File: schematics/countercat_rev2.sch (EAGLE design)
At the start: 32 parts, among them Q1 2N3904, Q2 IRF520, U2 74HC04_HEX_INVERTER, U3 USD-SOCKETNEW, U4 ATMEGA328P_PDIP, Y1 16MHz

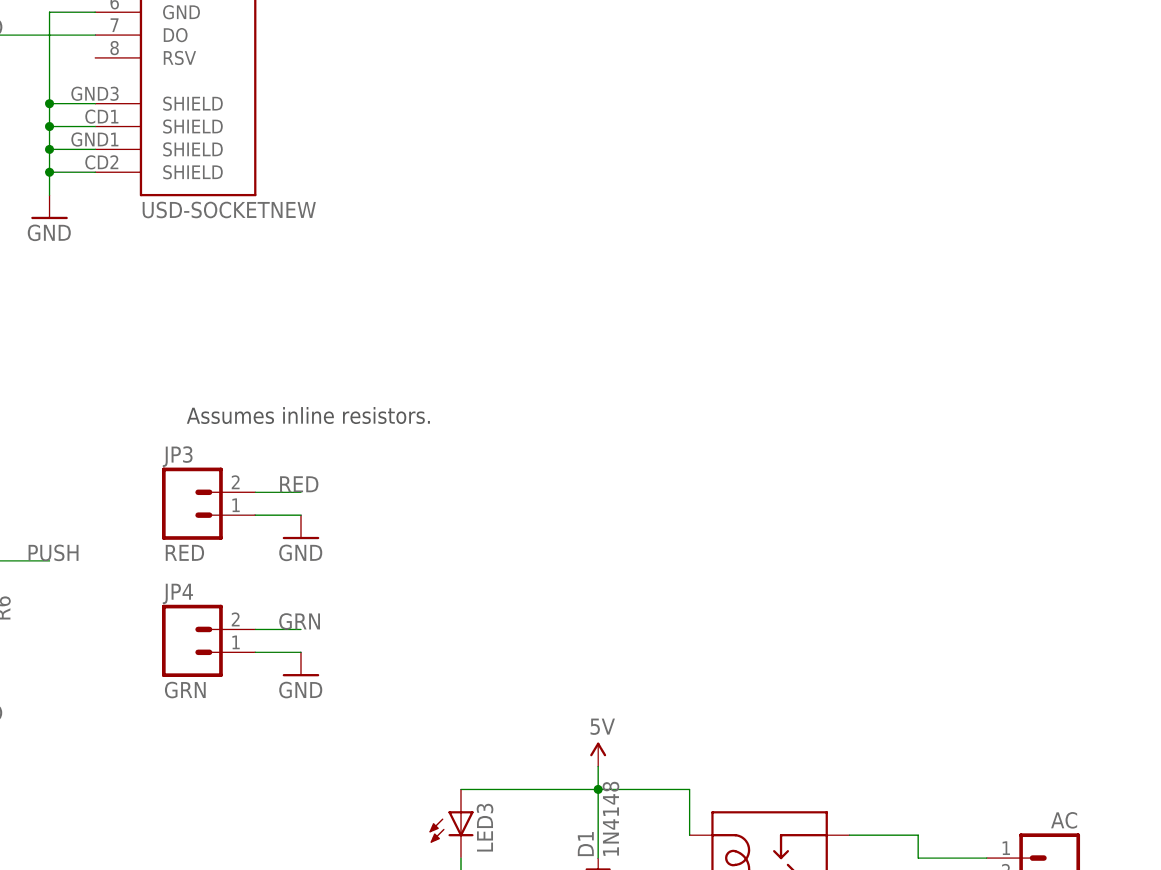
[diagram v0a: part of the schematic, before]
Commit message: Changed the LED hookup schematic
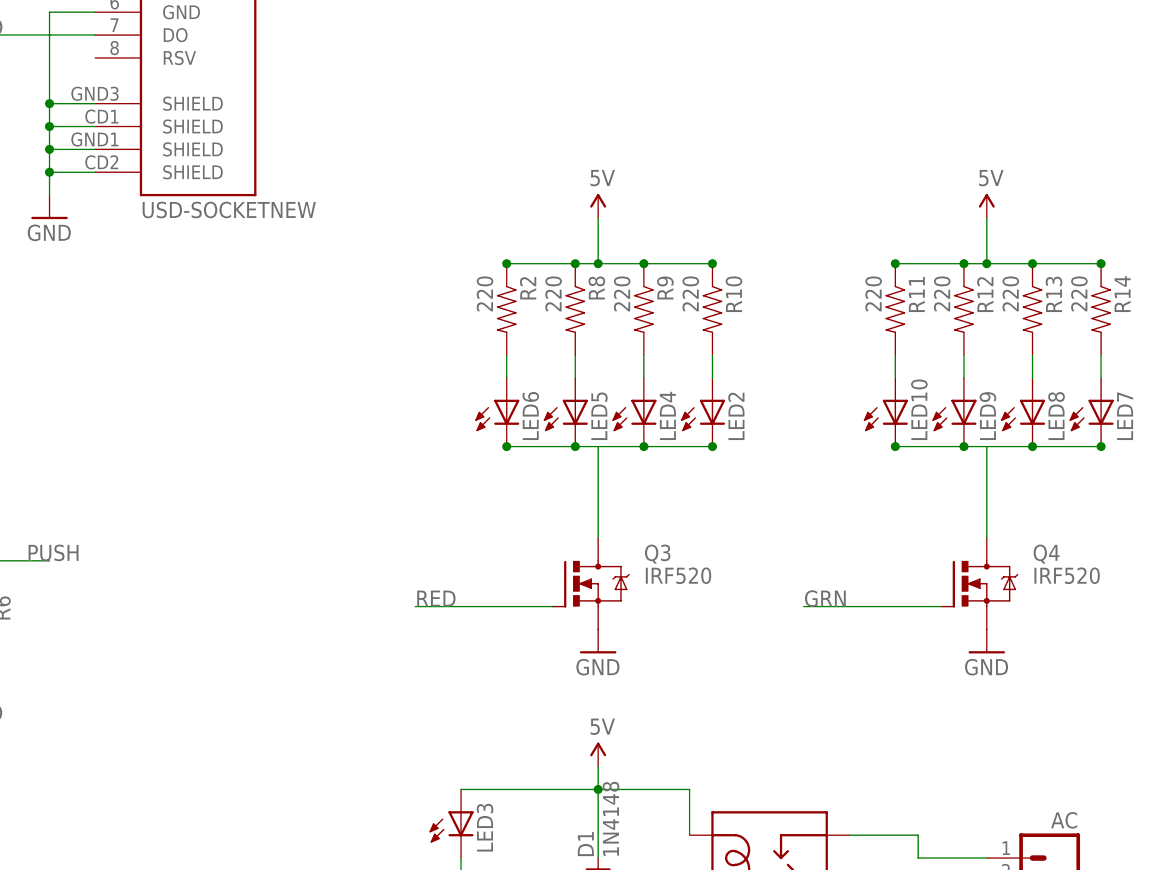
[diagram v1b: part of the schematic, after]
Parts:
- removed JP3: RED, SparkFun:M02POLAR
- removed JP4: GRN, SparkFun:M02POLAR
- added LED10, LED2, LED4, LED5, LED6, LED7, LED8, LED9: (no value), nick_DC2011:LED3MM
- added Q3, Q4: IRF520, transistor-power:IRF520
- added R10, R11, R12, R13, R14, R2, R8, R9: 220, SparkFun-Resistors:RESISTORPTH-1/4W
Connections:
- new net N$18: LED6.A, R2.2
- new net N$19: LED5.A, R8.2
- new net N$2: LED2.C, LED4.C, LED5.C, LED6.C, Q3.D
- new net N$21: LED4.A, R9.2
- new net N$22: LED2.A, R10.2
- new net N$23: LED10.C, LED7.C, LED8.C, LED9.C, Q4.D
- new net N$24: LED10.A, R11.2
- new net N$25: LED9.A, R12.2
- new net N$26: LED8.A, R13.2
- new net N$27: LED7.A, R14.2
- net 5V: now also R10.1, R11.1, R12.1, R13.1, R14.1, R2.1, R8.1, R9.1
- net GND: now also Q3.S, Q4.S; no longer JP3.1, JP4.1
- net GRN: now also Q4.G; no longer JP4.2
- net RED: now also Q3.G; no longer JP3.2
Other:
- note removed: "Assumes inline resistors."

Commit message: Started board design
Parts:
- removed C1, C4: .1uF, SparkFun-Capacitors:CAPPTH2
- removed D1: 1N4148, SparkFun:DIODEPTH
- removed LED1: Red, SparkFun-LED:LED3MM
- removed LED10, LED2, LED3, LED4, LED5, LED6, LED7, LED8, LED9: (no value), nick_DC2011:LED3MM
- removed LM7805: 5v, SparkFun-PowerIC:V_REG_78XXSINK
- removed MCP1700-3302E: 3.3v, SparkFun-PowerIC:V_REG_78XXTO-92_UNTESTED
- removed Q1: 2N3904, SparkFun:TRANSISTOR_NPNTO92
- removed Q2: IRF520, transistor-power:IRF520
- removed R1, R3, R5: 1k, SparkFun-Resistors:RESISTORPTH-1/4W
- removed R4: 10k, SparkFun-Resistors:RESISTORPTH-1/4W
- removed U$2: RELAYPTH3, SparkFun:RELAYPTH3
- removed U2: 74HC04_HEX_INVERTER, SparkFun-DigitalIC:74HC04_HEX_INVERTER
- removed U3: USD-SOCKETNEW, SparkFun:USD-SOCKETNEW
- added JP11: GRN1, SparkFun:M02POLAR
- added JP12: GRN2, SparkFun:M02POLAR
- added JP13: GRN3, SparkFun:M02POLAR
- added JP14: GRN4, SparkFun:M02POLAR
- added JP3: RED1, SparkFun:M02POLAR
- added JP4: RED2, SparkFun:M02POLAR
- JP2: value AC -> RELAY; device NickDC2011Breakouts:M025MM -> SparkFun:M03POLAR
- JP7: value VC0706 -> RED3; device SparkFun-Connectors:M04POLAR -> SparkFun:M02POLAR
- JP8: value FLASH -> RED4
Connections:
- removed net 3.3V: C4.1, LED1.A, MCP1700-3302E.OUT, U2.VCC, U3.VCC
- removed net N$1: LED3.C, R3.1
- removed net N$10: D1.A, Q1.C, R3.2, U$2.COIL2
- removed net N$11: Q1.B, R4.1, R5.2
- removed net N$14: LED1.C, R1.2
- removed net N$17: U2.5Y, U2.6A
- removed net N$20: U2.2Y, U3.CS
- removed net N$23: LED10.C, LED7.C, LED8.C, LED9.C, Q4.D
- removed net N$24: LED10.A, R11.2
- removed net N$25: LED9.A, R12.2
- removed net N$26: LED8.A, R13.2
- removed net N$27: LED7.A, R14.2
- removed net N$6: JP2.1, U$2.NC
- removed net N$9: JP2.2, U$2.NO
- removed net VB: JP10.2, LM7805.IN
- net 5V: now also JP10.2, JP2.1; no longer C1.1, D1.C, JP7.4, JP8.1, LED3.A, LM7805.OUT, MCP1700-3302E.IN, U$2.COIL1
- net FLASH: no longer Q2.G
- net GND: now also JP2.2; no longer C1.2, C4.2, JP7.3, LM7805.GND, MCP1700-3302E.GND, Q1.E, Q2.S, R1.1, R4.2, U2.GND, U3.GND, U3.SHIELD@1, U3.SHIELD@2, U3.SHIELD@3, U3.SHIELD@4
- net N$13: now also JP12.2, R12.2; no longer U2.4Y, U3.DI
- net N$15: now also JP13.2, R13.2; no longer U2.6Y, U3.SCK
- net N$16: now also JP14.2, R14.2; no longer U2.3Y, U2.4A
- net N$18: now also JP3.2; no longer LED6.A
- net N$19: now also JP4.2; no longer LED5.A
- net N$2: now also JP3.1, JP4.1, JP7.1, JP8.1; no longer LED2.C, LED4.C, LED5.C, LED6.C
- net N$21: now also JP7.2; no longer LED4.A
- net N$22: now also JP8.2; no longer LED2.A
- net N$4: now also JP11.1, JP12.1, JP13.1, JP14.1; no longer JP8.2, Q2.D
- net N$5: now also JP11.2, R11.2; no longer U2.1Y, U2.2A
- net RELAY: now also JP2.3; no longer R5.1
- net SFW_RXI: no longer JP7.1
- net SFW_TXO: no longer JP7.2
- net SPI_CS: no longer U2.1A
- net SPI_MISO: no longer U3.DO
- net SPI_MOSI: no longer U2.3A
- net SPI_SCK: no longer U2.5A
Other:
- note removed: "Attach 12 IR LEDs in parallel"
- note removed: "CAMERA"
- note removed: "Power Indicator"
- moved on the sheet: JP8, Q4, R10, R11, R12, R13, R14, R2, R8, R9

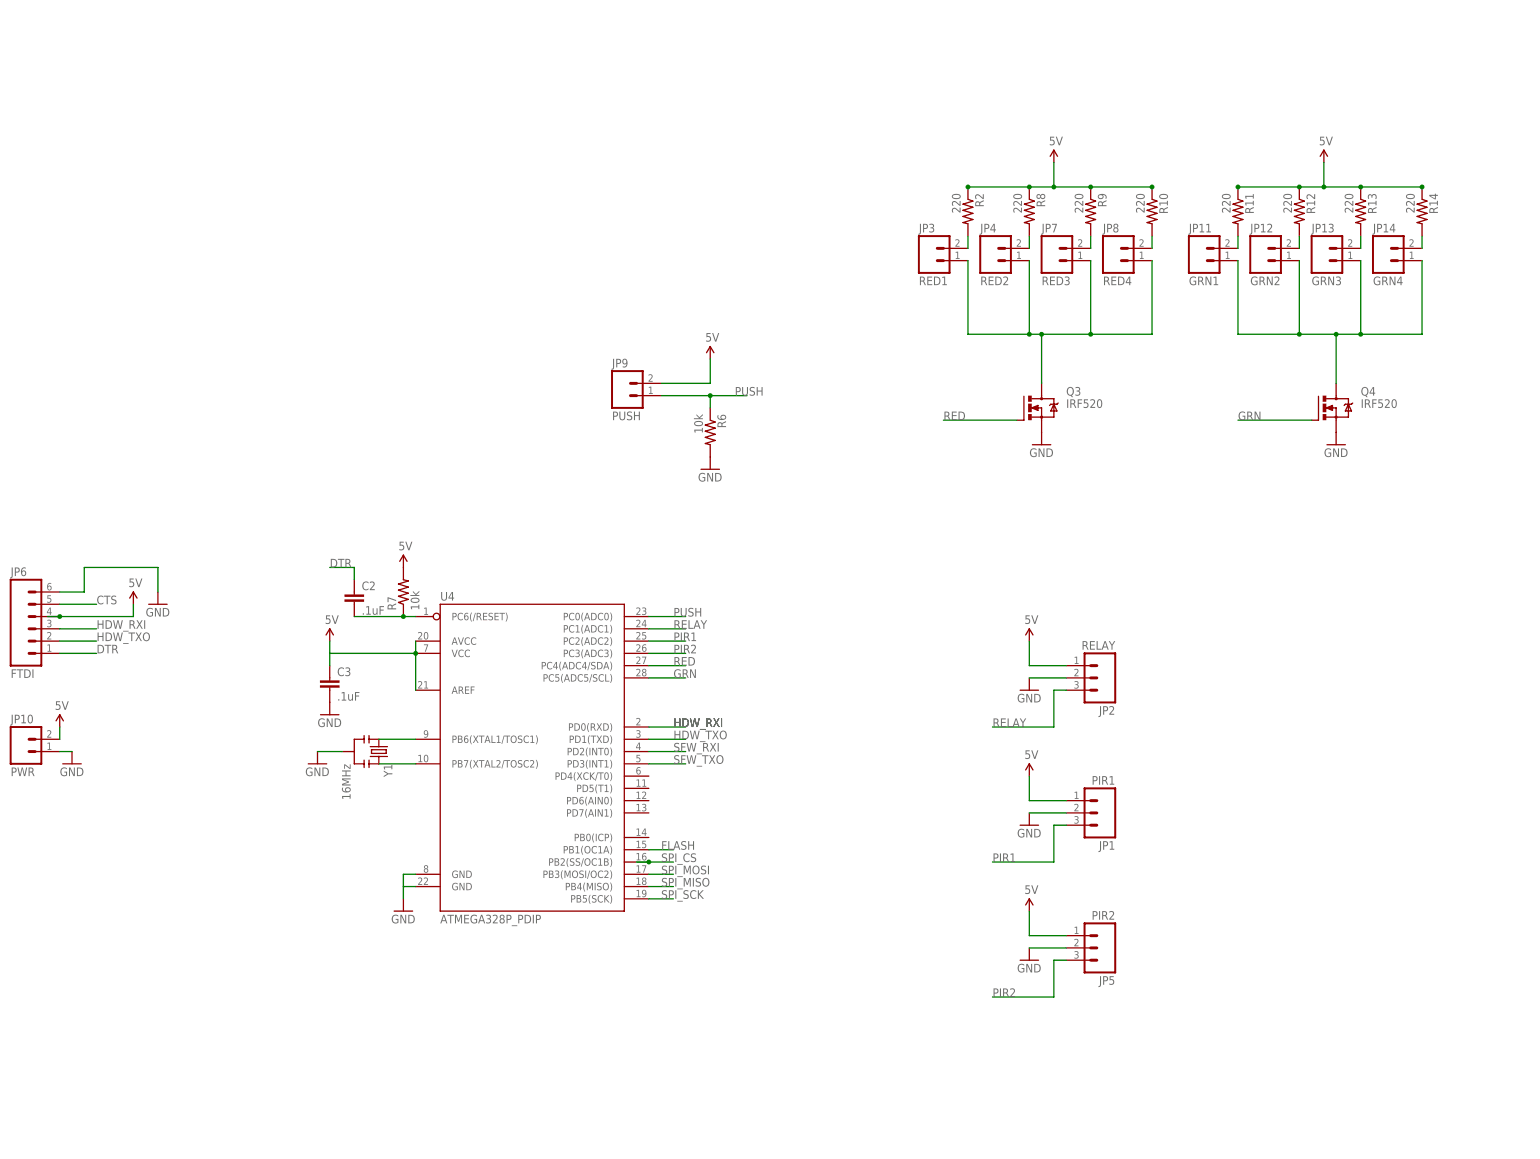
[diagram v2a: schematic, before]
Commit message: Changed board size, add shifter
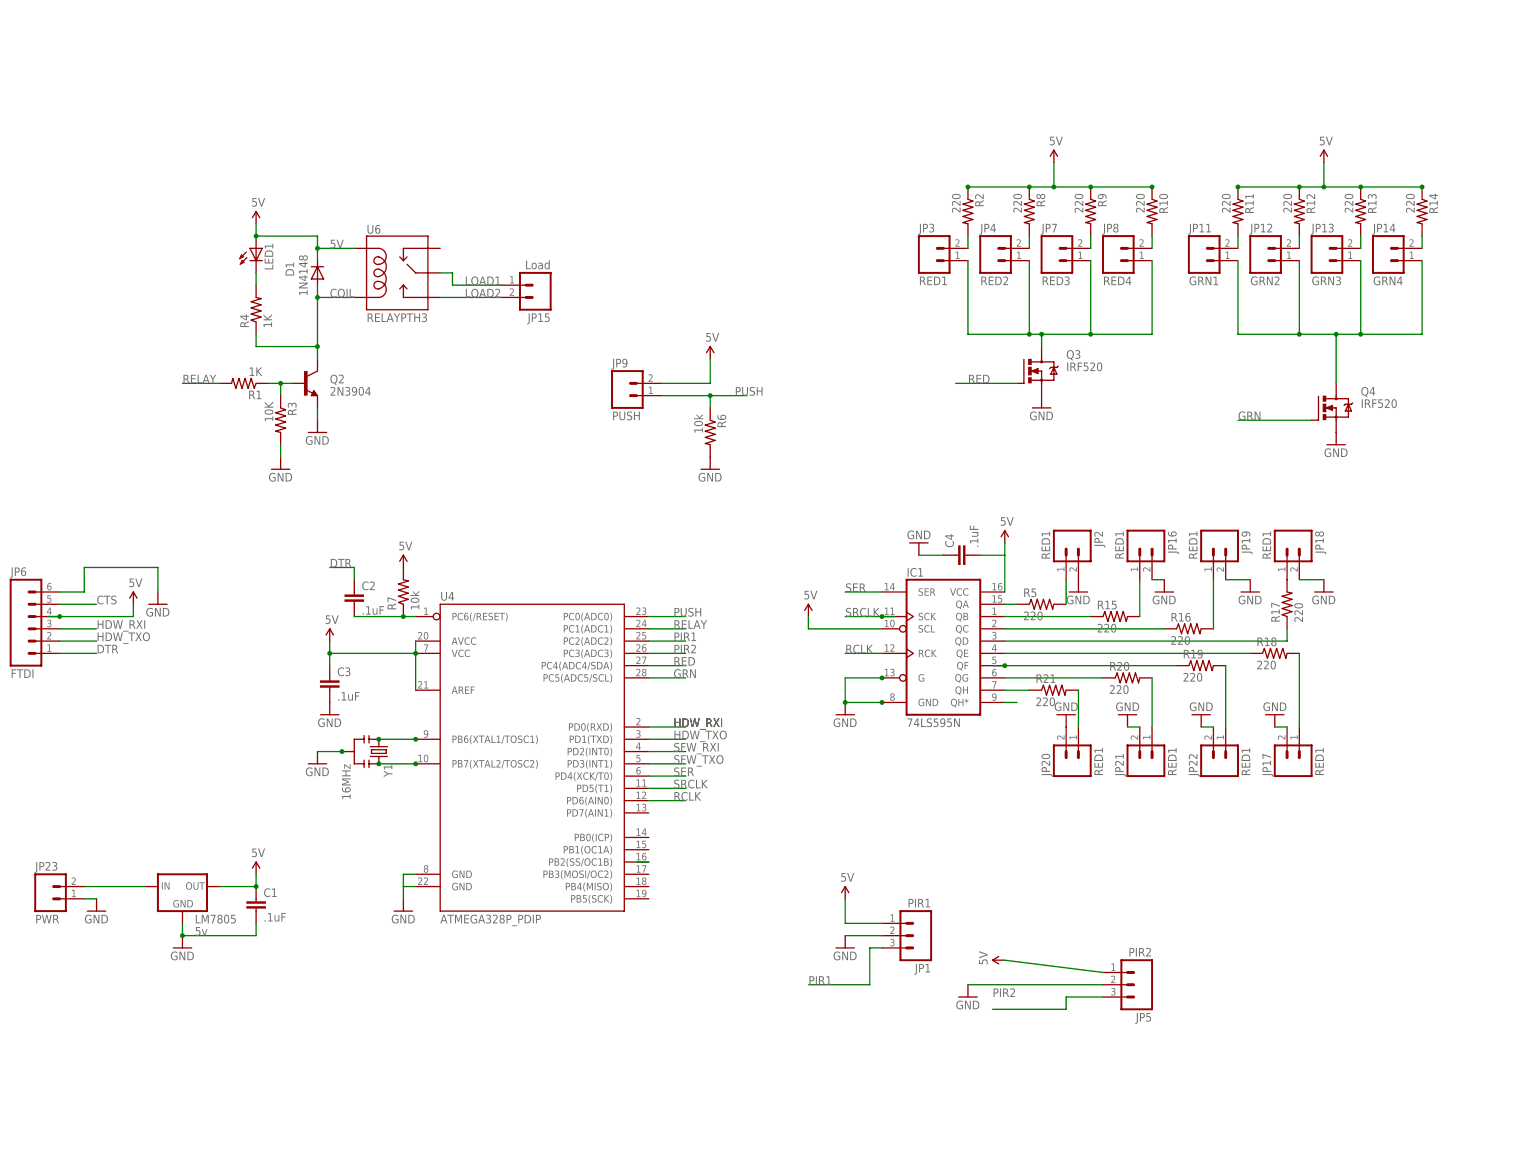
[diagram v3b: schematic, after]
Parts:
- removed JP10: PWR, SparkFun:M02POLAR
- added C1, C4: .1uF, SparkFun-Capacitors:CAPPTH2
- added D1: 1N4148, SparkFun:DIODE1N4148
- added IC1: 74LS595N, SparkFun-DigitalIC:74LS595N
- added JP15: Load, SparkFun:M025MM
- added JP16, JP17, JP18, JP19, JP20, JP21, JP22: RED1, SparkFun:M02POLAR
- added JP23: PWR, SparkFun:M02POLAR
- added LED1: (no value), SparkFun:LED5MM
- added LM7805: 5v, SparkFun-PowerIC:V_REG_78XXSINK
- added Q2: 2N3904, SparkFun:TRANSISTOR_NPNTO92
- added R1, R4: 1K, SparkFun-Resistors:RESISTORPTH-1/4W
- added R15, R16, R17, R18, R19, R20, R21, R5: 220, SparkFun-Resistors:RESISTORPTH-1/4W
- added R3: 10K, SparkFun-Resistors:RESISTORPTH-1/4W
- added U6: RELAYPTH3, SparkFun:RELAYPTH3
- JP2: value RELAY -> RED1; device SparkFun:M03POLAR -> SparkFun:M02POLAR
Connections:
- removed net FLASH: U4.PB1(OC1A)
- removed net N$12: C3.1
- removed net SPI_MISO: U4.PB4(MISO)
- removed net SPI_MOSI: U4.PB3(MOSI/OC2)
- removed net SPI_SCK: U4.PB5(SCK)
- new net COIL: D1.A, Q2.C, R4.1, U6.COIL2
- new net LOAD1: JP15.1, U6.MAIN
- new net LOAD2: JP15.2, U6.NO
- new net N$1: IC1.QH*
- new net N$10: JP2.1, R5.2
- new net N$11: JP16.1, R15.2
- new net N$14: JP19.1, R16.2
- new net N$17: JP18.1, R17.2
- new net N$20: JP17.1, R18.2
- new net N$23: JP22.1, R19.2
- new net N$24: JP21.1, R20.2
- new net N$25: JP20.1, R21.2
- new net N$26: IC1.QA, R5.1
- new net N$27: IC1.QB, R15.1
- new net N$28: IC1.QC, R16.1
- new net N$29: IC1.QD, R17.1
- new net N$30: IC1.QE, R18.1
- new net N$31: IC1.QF, R19.1
- new net N$32: IC1.QG, R20.1
- new net N$33: IC1.QH, R21.1
- new net N$6: Q2.B, R1.1, R3.1
- new net N$9: LED1.C, R4.2
- new net RCLK: IC1.RCK, U4.PD6(AIN0)
- new net SER: IC1.SER, U4.PD4(XCK/T0)
- new net SRCLK: IC1.SCK, U4.PD5(T1)
- new net VB: JP23.2, LM7805.IN
- net 5V: now also C1.1, C4.2, D1.C, IC1.SCL, IC1.VCC, LED1.A, LM7805.OUT, U6.COIL1; no longer JP10.2, JP2.1
- net GND: now also C1.2, C4.1, IC1.G, IC1.GND, JP16.2, JP17.2, JP18.2, JP19.2, JP20.2, JP21.2, JP22.2, JP23.1, LM7805.GND, Q2.E, R3.2; no longer JP10.1
- net N$8: now also C3.1
- net RELAY: now also R1.2; no longer JP2.3
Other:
- moved on the sheet: JP1, JP5, Q3

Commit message: Updated board and schematic
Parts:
- removed R10, R12, R13, R14, R15, R16, R17, R18, R19, R20, R21, R5: 220, SparkFun-Resistors:RESISTORPTH-1/4W
- added BLU, GRN, RED, YLW: (no value), SparkFun-LED:LED3MM
- added C5: .1uF, SparkFun-Capacitors:CAPPTH2
- added JP10: RED_RAW, SparkFun:M02POLAR
- added JP24: GRN_RAW, SparkFun:M02POLAR
- added JP25: BLU1, SparkFun:M02POLAR
- added JP26: BLU2, SparkFun:M02POLAR
- added JP27: BLU3, SparkFun:M02POLAR
- added JP28: BLU4, SparkFun:M02POLAR
- added JP29: BLU_RAW, SparkFun:M02POLAR
- added JP30: YLW1, SparkFun:M02POLAR
- added JP31: YLW2, SparkFun:M02POLAR
- added JP32: YLW3, SparkFun:M02POLAR
- added JP33: YLW4, SparkFun:M02POLAR
- added JP34: YLW_RAW, SparkFun:M02POLAR
- added JP35: AUX, SparkFun-Connectors:M08LOCK
- added JP36: AUX_PWR, SparkFun:M02POLAR
- added Q1, Q5: IRF520, transistor-power:IRF520
- added R35: R-GRN, SparkFun-Resistors:RPACK-BUSSED-5-SIP-PTH-5
- JP16: value RED1 -> SHF3
- JP17: value RED1 -> SHF5
- JP18: value RED1 -> SHF1
- JP19: value RED1 -> SHF2
- JP2: value RED1 -> SHF4
- JP20: value RED1 -> SHF8
- JP21: value RED1 -> SHF7
- JP22: value RED1 -> SHF6
- R11: value 220 -> R-SHF; device SparkFun-Resistors:RESISTORPTH-1/4W -> SparkFun-Resistors:RPACK-BUSSED-8-SIP-PTH-8
- R2: value 220 -> R-RED; device SparkFun-Resistors:RESISTORPTH-1/4W -> SparkFun-Resistors:RPACK-BUSSED-5-SIP-PTH-5
- R8: value 220 -> R-BLU; device SparkFun-Resistors:RESISTORPTH-1/4W -> SparkFun-Resistors:RPACK-BUSSED-5-SIP-PTH-5
- R9: value 220 -> R-YLW; device SparkFun-Resistors:RESISTORPTH-1/4W -> SparkFun-Resistors:RPACK-BUSSED-5-SIP-PTH-5
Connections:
- removed net N$22 (its old number): JP8.2, R10.2
- removed net SFW_RXI: U4.PD2(INT0)
- removed net SFW_TXO: U4.PD3(INT1)
- new net B0: JP35.3, U4.PB0(ICP)
- new net B1: JP35.4, U4.PB1(OC1A)
- new net BLU: Q3.G, U4.PD2(INT0)
- new net D7: JP35.2, U4.PD7(AIN1)
- new net N$12: JP4.2, R2.3
- new net N$18: JP7.2, R2.4
- new net N$34: BLU.C, JP25.1, JP26.1, JP27.1, JP28.1, JP29.1, Q3.D
- new net N$35: JP26.2, R8.3
- new net N$36: JP27.2, R8.4
- new net N$37: JP28.2, R8.5
- new net N$38: BLU.A, R8.6
- new net N$39: JP25.2, R8.2
- new net N$40: JP30.1, JP31.1, JP32.1, JP33.1, JP34.1, Q5.D, YLW.C
- new net N$41: JP31.2, R9.3
- new net N$42: JP32.2, R9.4
- new net N$43: JP33.2, R9.5
- new net N$44: R9.6, YLW.A
- new net N$45: GRN.A, R35.6
- new net N$46: JP30.2, R9.2
- new net SPI_MISO: JP35.7, U4.PB4(MISO)
- new net SPI_MOSI: JP35.6, U4.PB3(MOSI/OC2)
- new net SPI_SCK: JP35.8, U4.PB5(SCK)
- new net YLW: Q5.G, U4.PD3(INT1)
- net 5V: now also JP10.2, JP24.2, JP29.2, JP34.2, JP36.1, R35.1; no longer JP6.4, R10.1, R11.1, R12.1, R13.1, R14.1
- net GND: now also C5.2, JP35.1, JP36.2, Q1.S, Q5.S, R11.1; no longer JP16.2, JP17.2, JP18.2, JP19.2, JP2.2, JP20.2, JP21.2, JP22.2
- net N$1: now also IC1.QE, JP17.1; no longer IC1.QH*
- net N$10: now also JP18.2, R11.2; no longer JP2.1, R5.2
- net N$11: now also JP19.2, R11.3; no longer JP16.1, R15.2
- net N$13: now also R35.3; no longer R12.2
- net N$14: now also JP16.2, R11.4; no longer JP19.1, R16.2
- net N$15: now also R35.4; no longer R13.2
- net N$16: now also R35.5; no longer R14.2
- net N$17: now also JP2.2, R11.5; no longer JP18.1, R17.2
- net N$19: now also JP8.2, R2.5; no longer JP4.2, R8.2
- net N$2: now also JP10.1, Q1.D, RED.C; no longer Q3.D
- net N$20: now also JP17.2, R11.6; no longer JP17.1, R18.2
- net N$21: now also R2.6, RED.A; no longer JP7.2, R9.2
- net N$23: now also JP22.2, R11.7; no longer JP22.1, R19.2
- net N$24: now also JP21.2, R11.8; no longer JP21.1, R20.2
- net N$25: now also JP20.2, R11.9; no longer JP20.1, R21.2
- net N$26: now also JP18.1; no longer R5.1
- net N$27: now also JP19.1; no longer R15.1
- net N$28: now also JP16.1; no longer R16.1
- net N$29: now also JP2.1; no longer R17.1
- net N$30: now also IC1.QG, JP21.1; no longer IC1.QE, R18.1
- net N$31: now also JP22.1; no longer R19.1
- net N$32: now also IC1.QH, JP20.1; no longer IC1.QG, R20.1
- net N$33: now also JP6.4; no longer IC1.QH, R21.1
- net N$4: now also GRN.C, JP24.1, Q4.D
- net N$5: now also R35.2; no longer R11.2
- net RED: now also Q1.G; no longer Q3.G
- net SPI_CS: now also JP35.5
- net VB: now also C5.1
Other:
- note added: "Shift Module"
- moved on the sheet: C4, IC1, JP1, JP16, JP17, JP18, JP19, JP2, JP20, JP21, JP22, JP3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
